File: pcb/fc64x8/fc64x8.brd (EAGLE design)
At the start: 20.3 x 31.8 mm, 42 parts, among them J1 Micro USB, J2 Outputs, U1 MK20DX128VLF5, U2 AAT3110IGU-5.0-T1, U3 SN74HCT245PWR, X1 16 MHz

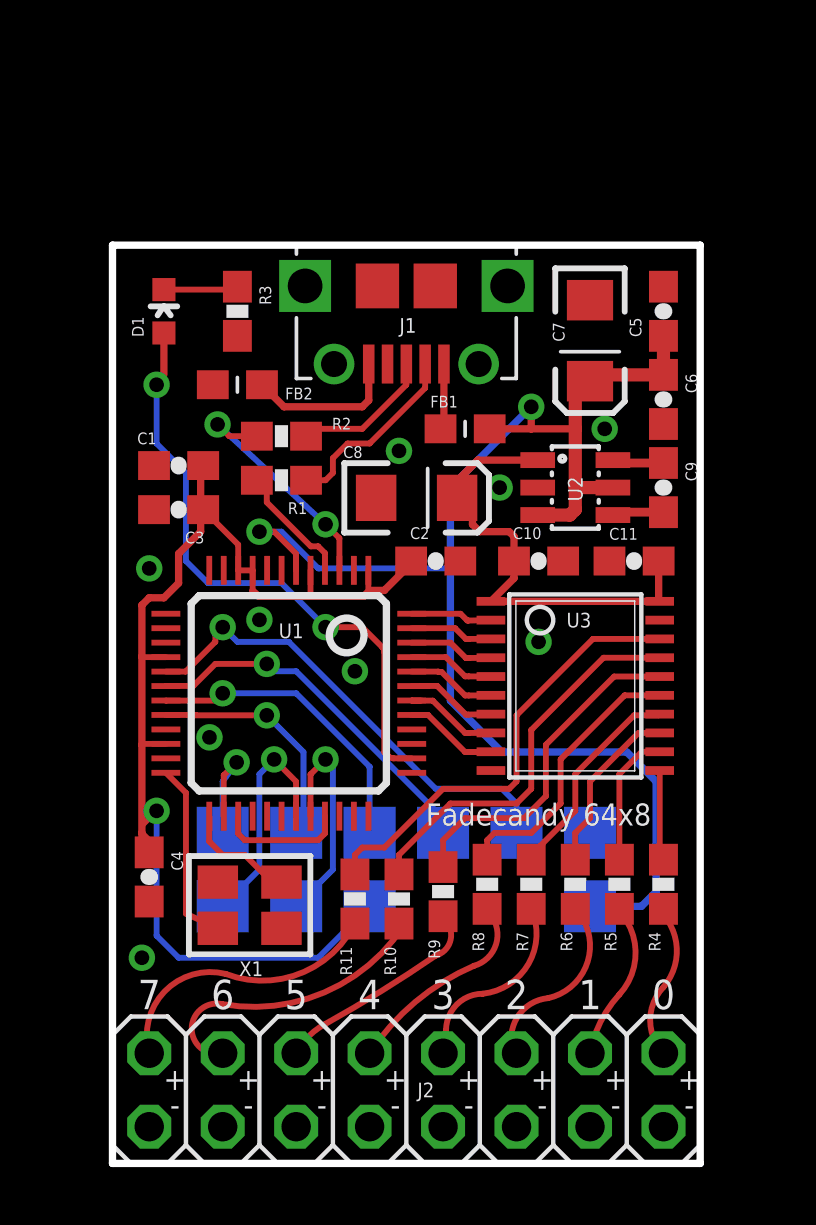
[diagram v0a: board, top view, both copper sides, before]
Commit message: Draft of Revision B PCB layout
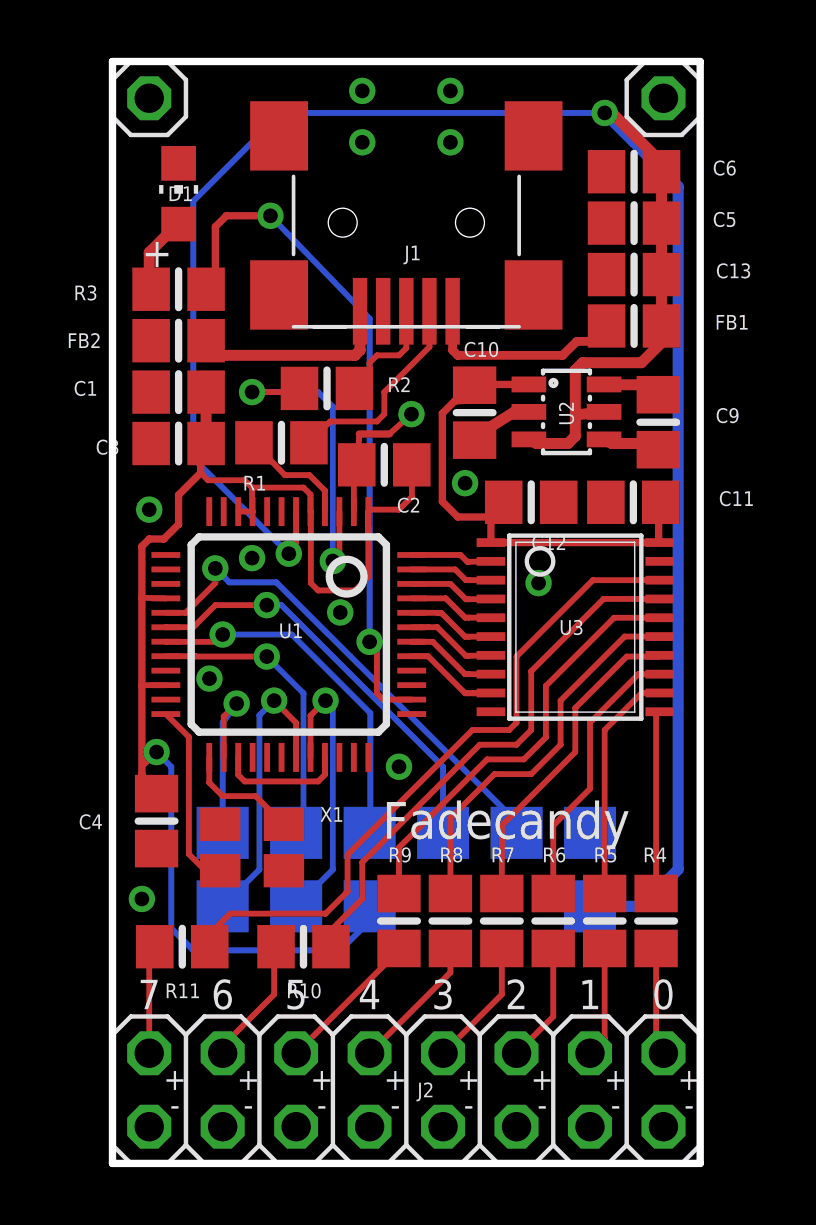
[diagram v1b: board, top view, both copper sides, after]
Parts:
- removed C7, C8: 10uF, SparkFun-Passives:EIA3216
- added C12, C13: 10uF, scanlime:0805
- added JP1, JP2: (no value), pinhead:1X01
- C1, C10, C11, C2, C3, C4, C5, C6, C9: device SparkFun-Passives:0603-CAP -> scanlime:0805
- D1: device SparkFun-LED:LED-0603 -> adafruit:CHIP-LED0805
- FB1, FB2: value (none) -> FB0805/NO-OUTLINE; device scanlime:0603 -> scanlime:0805
- J1: value Micro USB -> (none); device scanlime:FCI-10118194 -> scanlime:USB-MINIB
- R1, R10, R11, R2, R3, R4, R5, R6, R7, R8, R9: device SparkFun-Passives:0603-RES -> scanlime:0805
- moved C6 7.94 mm to (18.0, 34.3), turned to 180 degrees
- moved FB1 6.84 mm to (18.0, 29.0), turned to 0 degrees
- moved R11 6.19 mm to (2.41, 7.49), turned to 180 degrees
- moved J1 5.59 mm to (10.2, 33.5)
- moved C10 5.59 mm to (12.5, 26.0), turned to 270 degrees
- moved U$1 4.33 mm to (17.8, 33.8)
- moved D1 4.10 mm to (2.29, 33.5)
- moved C2 3.77 mm to (9.40, 24.2), turned to 180 degrees
- moved R10 3.69 mm to (6.60, 7.49), turned to 180 degrees
- moved C5 3.21 mm to (18.0, 32.5), turned to 180 degrees
- moved X1 2.97 mm to (4.83, 10.9)
- moved U2 2.63 mm to (15.7, 26.0)
- moved C1 2.54 mm to (2.29, 26.7)
- moved FB2 2.54 mm to (2.29, 28.4), turned to 180 degrees
- moved C3 2.29 mm to (2.29, 24.9)
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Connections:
- net +5V: now also C13.1, FB1.2; no longer C7.A, FB1.1
- net GND: now also C12.2, C13.2, D1.C, FB2.2, J1.GND1, J1.GND2, J1.GND3, J1.GND4, JP1.1, JP2.1; no longer C7.C, C8.C, FB2.1, J1.S1, J1.S2, J1.S3, J1.S4, J1.S5, J1.S6, R3.2
- net N$1: now also R3.1; no longer D1.A
- net N$10: now also J1.D+; no longer J1.3
- net N$27: now also C12.1; no longer C8.A
- net N$3: now also D1.A, R3.2; no longer D1.C, R3.1
- net N$5: now also FB1.1, J1.VBUS; no longer FB1.2, J1.1
- net N$7: now also FB2.1, J1.GND; no longer FB2.2, J1.5
- net N$9: now also J1.D-; no longer J1.2
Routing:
- net +5V: track 50.5 -> 78.7 mm
- net N$30: track 15.6 -> 23.1 mm
- net GND: track 0.00 -> 6.98 mm, vias 9 -> 13
- net +3V3: track 43.0 -> 49.3 mm
- net N$5: track 2.26 -> 7.35 mm
- net N$38: track 8.72 -> 3.76 mm
- net N$29: track 13.7 -> 18.6 mm
- net N$37: track 8.71 -> 4.45 mm
- net N$25: track 7.37 -> 11.1 mm
- net N$26: track 9.61 -> 13.3 mm
- net N$24: track 6.02 -> 9.54 mm
- net N$12: track 8.41 -> 11.9 mm
- net N$23: track 4.67 -> 8.09 mm
- net N$20: track 3.14 -> 6.34 mm
- net N$28: track 11.8 -> 14.9 mm
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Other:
- board size 20.3 x 31.8 mm -> 20.3 x 38.1 mm
- board text added: "LED Controller fc64x8 Rev B"
- board text removed: "Fadecandy 64x8"
- board text removed: "LED Controller"
- board text removed: "Rev A"

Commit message: Update fc64x8 CAD files with final design from Adafruit
- Remove outdated BOM file (Adafruit doesn't use a separate BOM spreadsheet)
- Added fiducials
- Added Adafruit logo
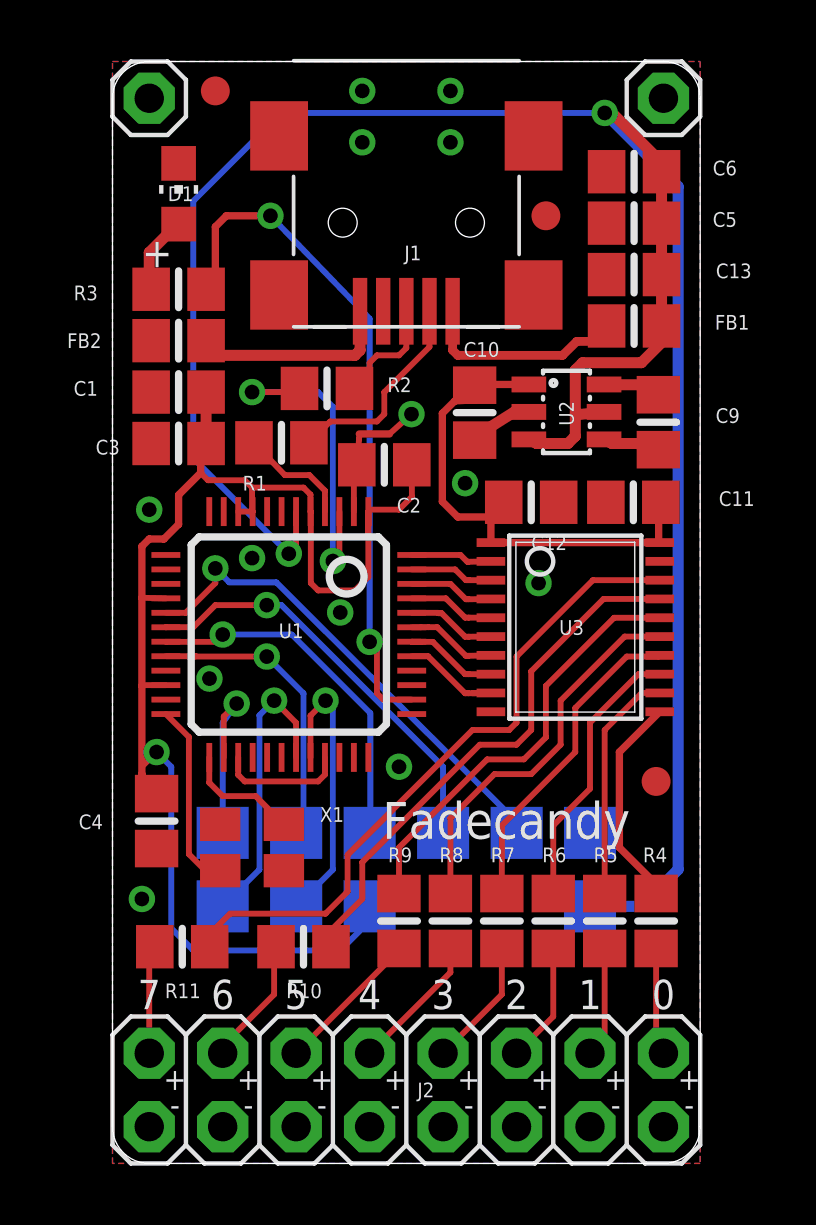
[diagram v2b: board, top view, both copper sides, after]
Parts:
- added FID1, FID2, FID3: FIDUCIAL"", microbuilder:FIDUCIAL_1MM
- added U$2: (no value), microbuilder:ADAFRUIT_TEXT_20MM
- C1, C5: value 2.2uF -> 10uF
- R10, R11, R4, R5, R6, R7, R8, R9: value 75 -> 68
- moved U$1 23.4 mm to (2.54, 16.0)
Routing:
- net N$20: track 6.34 -> 7.56 mm
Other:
- outline, holes or cut-outs redrawn
- board text added: "Manufactured by"
